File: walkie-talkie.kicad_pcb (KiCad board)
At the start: 2 copper layers, 50.5 x 74.5 mm, 12 parts, among them J1 I2C, J2 Conn_01x08, J3 esp32-pico-kit, J4 speakers, SW1 Transmit, SW2 POWER, U1 tp4056, U2 adafruit-MAX98357, U3 mems-mic

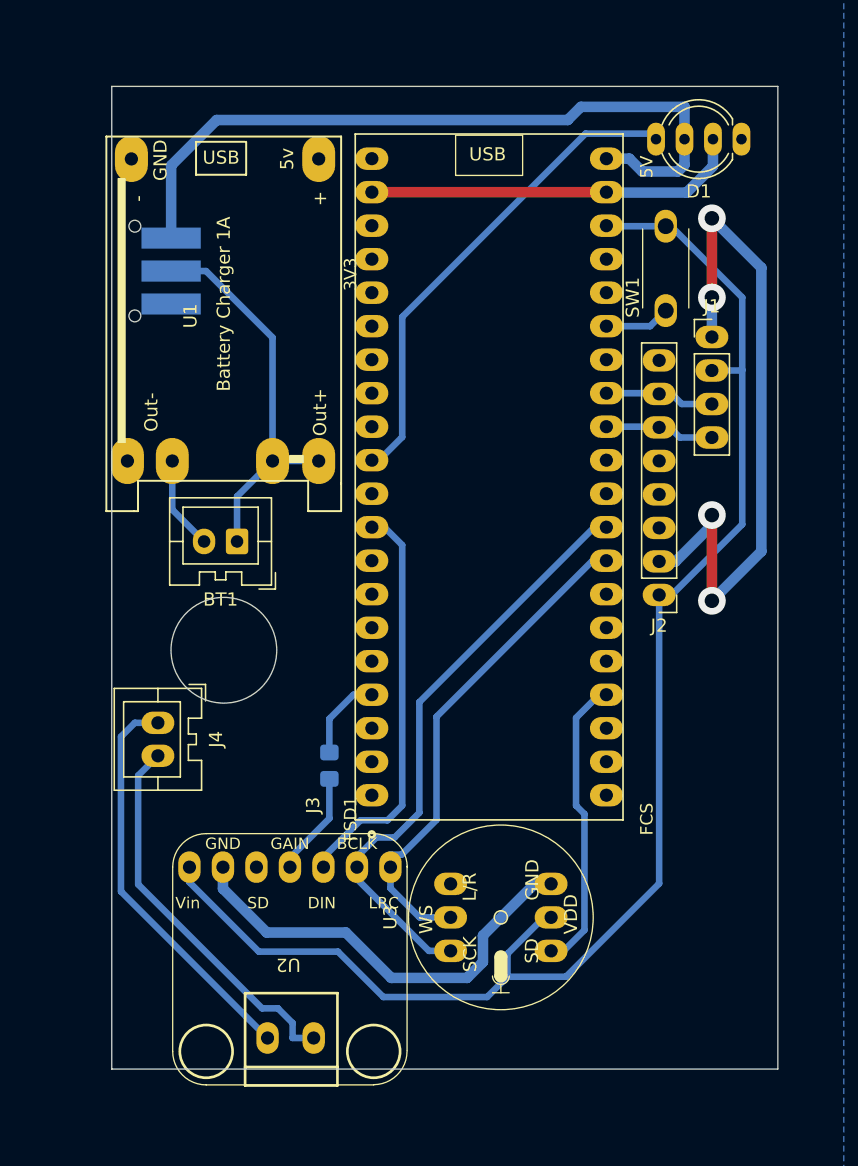
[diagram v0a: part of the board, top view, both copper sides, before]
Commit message: Add mounting holes
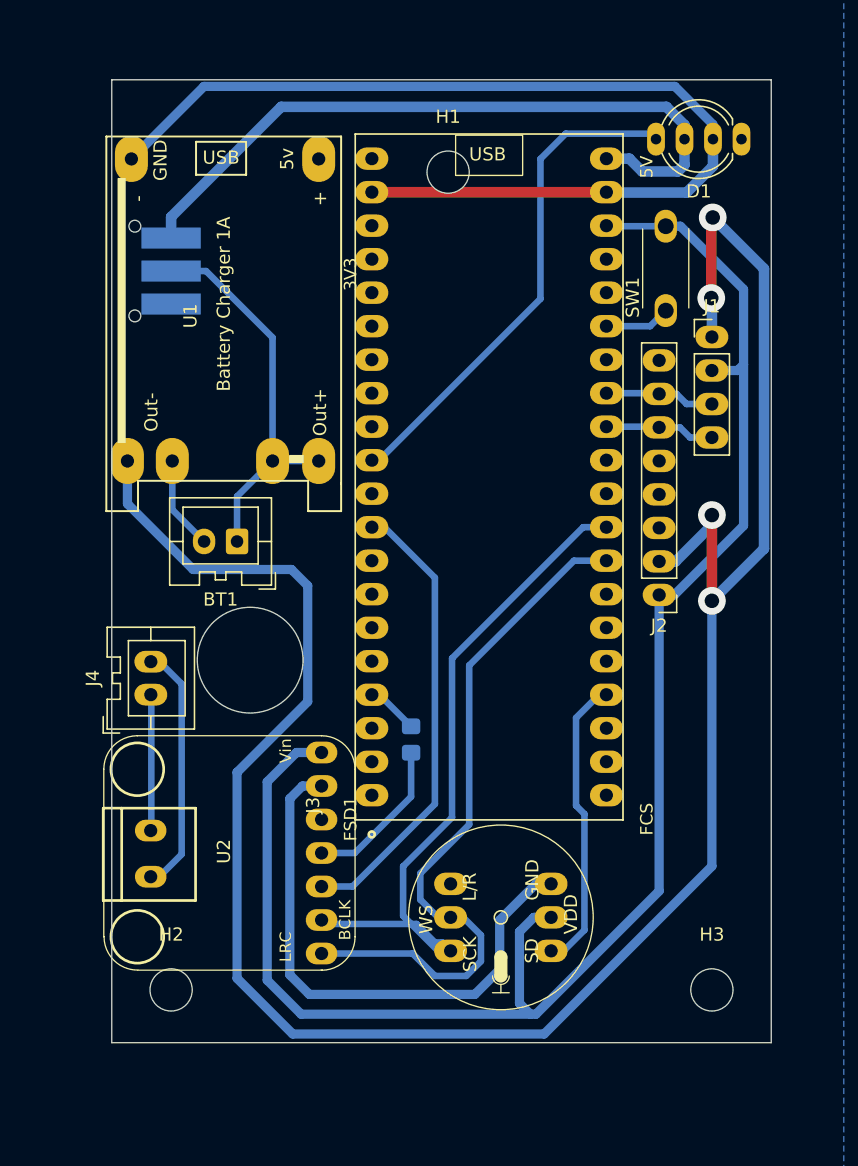
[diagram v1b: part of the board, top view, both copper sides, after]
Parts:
- added H1: MountingHole, MountingHole:MountingHole_3.2mm_M3, F.Cu at (68.0, 63.0)
- added H2: MountingHole, MountingHole:MountingHole_3.2mm_M3, F.Cu at (47.0, 125.0)
- added H3: MountingHole, MountingHole:MountingHole_3.2mm_M3, F.Cu at (88.0, 125.0)
- U1: value tp4056 -> WARNING: Switch off when Plugging in Power on the ESP
- moved U2 9.21 mm to (51.5, 114.5), turned to 90 degrees
- moved R1 6.50 mm to (65.2, 106.0)
- moved J4 2.20 mm to (45.5, 102.6), turned to 90 degrees
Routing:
- net GND: track 115.7 -> 288.1 mm
- net Net-(J4-Pin_1): track 30.7 -> 10.3 mm
- net I2S_RLCLK: track 38.2 -> 53.9 mm
- net +3V3: track 112.6 -> 128.1 mm
- net Net-(J4-Pin_2): track 29.2 -> 19.0 mm
- net I2S_BCLK: track 45.3 -> 52.3 mm
- net Net-(U2-GAIN): track 7.93 -> 11.9 mm
- net I2S_AMP_DATA: track 31.0 -> 34.7 mm
- net +5V: track 57.2 -> 54.1 mm
- net I2S_AMP_GAIN: track 6.53 -> 3.97 mm
- net Net-(D1-DIN): track 37.3 -> 38.2 mm
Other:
- board size 50.5 x 74.5 mm -> 50 x 73 mm

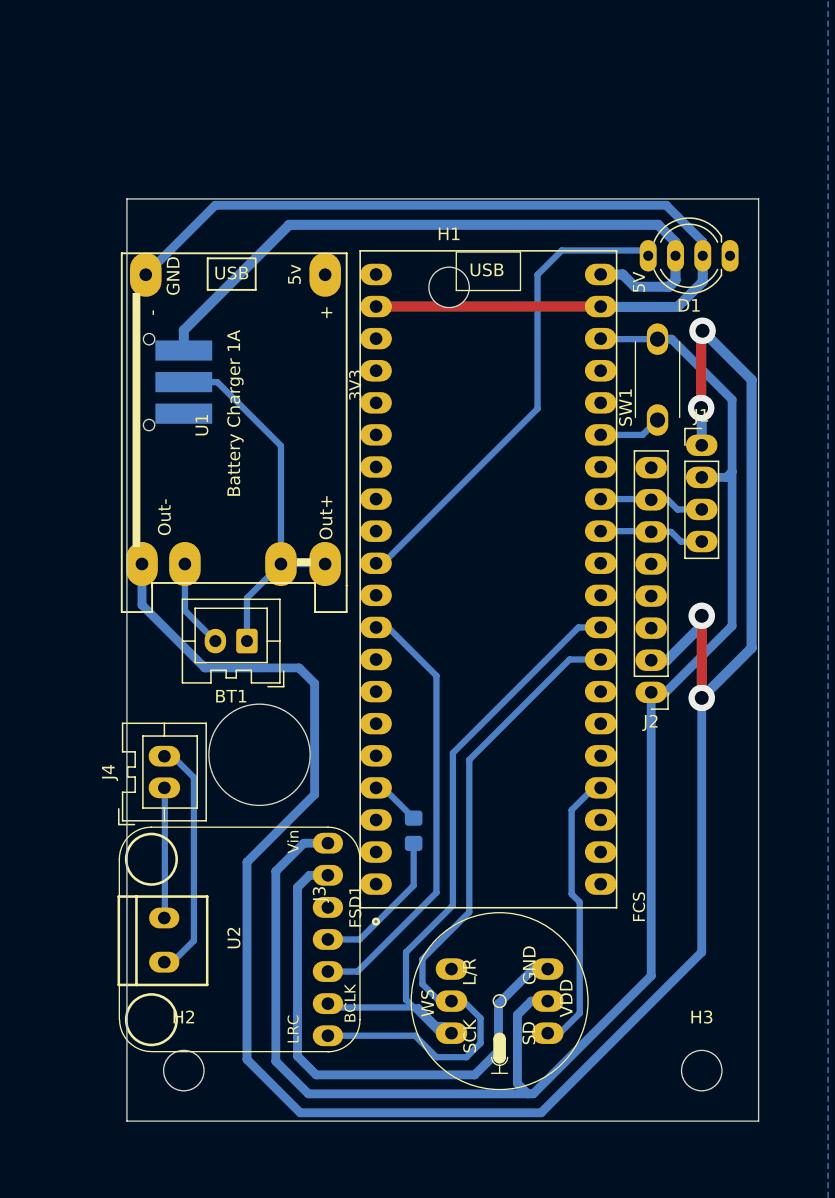
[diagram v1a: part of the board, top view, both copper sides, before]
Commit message: Add CVS speaker
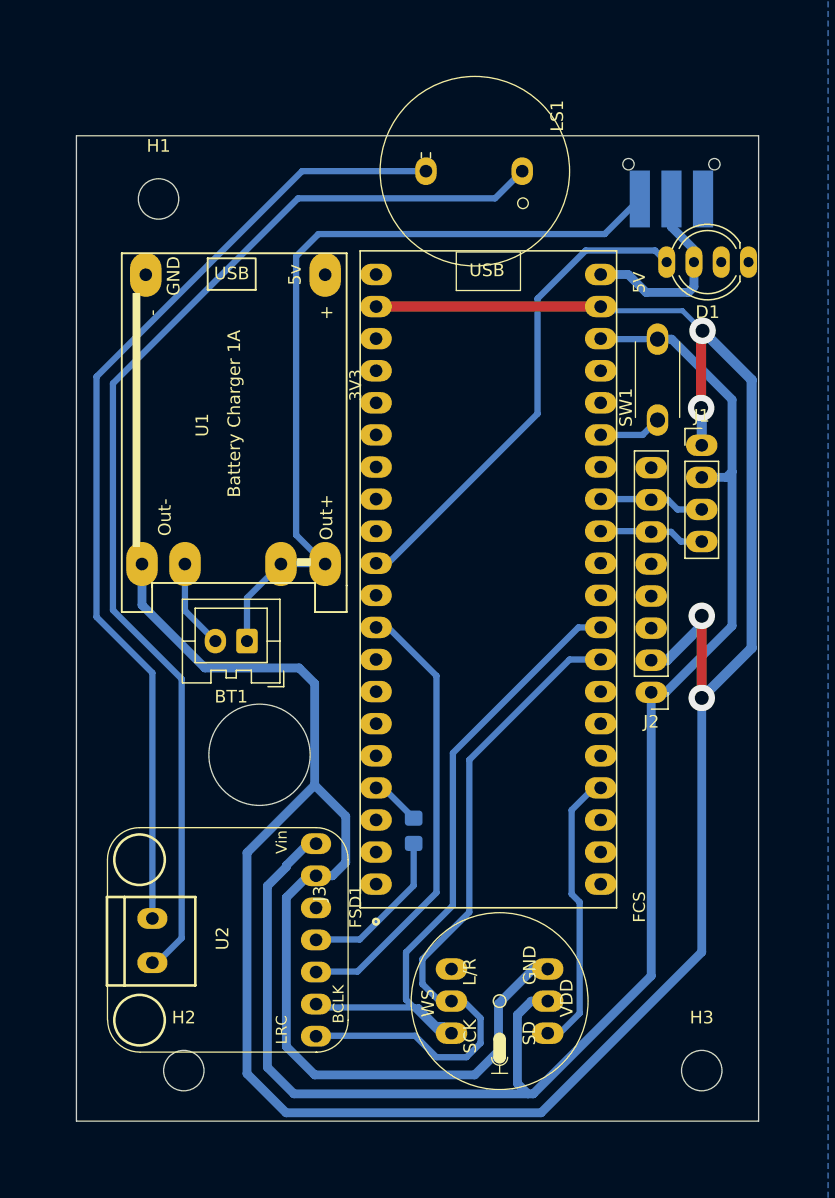
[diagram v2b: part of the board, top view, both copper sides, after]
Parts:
- removed J4: speakers, Connector_JST:JST_XA_B02B-XASK-1_1x02_P2.50mm_Vertical
- added LS1: Speaker, Connector_PinSocket_2.54mm:PinSocket_1x04_P2.54mm_Horizontal, F.Cu at (70.0, 53.8)
- moved SW2 44.8 mm to (85.6, 53.2), turned to 0 degrees
- moved H1 24.0 mm to (45.0, 56.0)
- moved D1 1.54 mm to (91.7, 61.0)
- moved U2 0.94 mm to (50.6, 114.5)
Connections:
- SW2 pad 1: unconnected-(SW2-A-Pad1) -> Net-(BT1-+)
- SW2 pad 2: Net-(BT1-+) -> +5V
- SW2 pad 3: +5V -> unconnected-(SW2-C-Pad3)
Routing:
- net Net-(U2-OUTP): track 19.0 -> 88.6 mm
- net Net-(U2-OUTN): track 10.3 -> 77.5 mm
- net GND: track 288.1 -> 248.4 mm
- net +5V: track 54.1 -> 15.8 mm
- net Net-(BT1-+): track 29.9 -> 65.1 mm
- net Net-(U2-GAIN): track 11.9 -> 12.8 mm
- net I2S_RLCLK: track 53.9 -> 54.9 mm
- net I2S_AMP_DATA: track 34.7 -> 35.7 mm
- net I2S_BCLK: track 52.3 -> 53.3 mm
- net Net-(D1-DIN): track 38.2 -> 39.0 mm
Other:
- board size 50 x 73 mm -> 54 x 78 mm

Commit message: Lolin32-Lite PCB
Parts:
- removed BT1: Battery_Cell, Connector_JST:JST_XA_B02B-XASK-1_1x02_P2.50mm_Vertical
- removed J2: Conn_01x08, Connector_PinHeader_2.54mm:PinHeader_1x08_P2.54mm_Vertical
- removed J3: esp32-pico-kit, esp32-pico-kit:esp32-pico-kit
- SW1: value Transmit -> POWER; footprint pts636:pts636 -> Button_Switch_SMD:SW_SPDT_CK-JS102011SAQN; moved to B.Cu
- SW2: value POWER -> Transmit; footprint Button_Switch_SMD:SW_SPDT_CK-JS102011SAQN -> pts636:pts636
- U1: value WARNING: Switch off when Plugging in Power on the ESP -> ~; footprint tp4056:tp4056 -> lolin32-lite:lolin32-lite
- moved H2 161.8 mm to (202.7, 81.0)
- moved U2 98.9 mm to (139.6, 71.7), turned to -90 degrees
- moved R1 73.1 mm to (129.8, 71.7)
- moved U3 71.7 mm to (137.9, 91.1), turned to 0 degrees
- moved H1 71.1 mm to (116.0, 59.0)
- moved LS1 67.8 mm to (137.9, 54.3)
- moved H3 65.7 mm to (147.0, 96.0)
- moved U1 65.0 mm to (116.0, 71.5), turned to 0 degrees
- moved SW2 62.2 mm to (147.4, 59.9), turned to 90 degrees
- moved D1 58.8 mm to (148.8, 46.7)
- moved SW1 39.9 mm to (116.3, 97.7), turned to 180 degrees
- moved J1 22.3 mm to (104.5, 90.5)
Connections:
- D1 pad 3: +5V -> +3V3
- SW1 pad 1: Net-(J3-IO2) -> +3V3
- SW1 pad 2: +3V3 -> Net-(SW1-B)
- SW2 pad 1: Net-(BT1-+) -> Net-(U1-IO22)
- SW2 pad 2: +5V -> +3V3
- U1 pad 1: VBUS -> unconnected-(U1-I36-Pad1)
- U1 pad 2: GND -> unconnected-(U1-I39-Pad2)
- U1 pad 3: Net-(BT1-+) -> Net-(SW1-B)
- U1 pad 4: Net-(BT1--) -> unconnected-(U1-I34-Pad4)
- U1 pad 5: Net-(BT1-+) -> unconnected-(U1-I35-Pad5)
- U1 pad 6: GND -> unconnected-(U1-IO32-Pad6)
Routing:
- net GND: track 248.4 -> 101.8 mm, vias 4 -> 6
- net Net-(U2-OUTP): track 88.6 -> 17.1 mm
- net Net-(BT1-+): track 65.1 -> 0.00 mm
- net Net-(U2-OUTN): track 77.5 -> 23.8 mm
- net Net-(U1-IO22): track 0.00 -> 47.0 mm
- net Net-(SW1-B): track 0.00 -> 41.2 mm
- net I2S_AMP_DATA: track 35.7 -> 5.34 mm
- net I2S_BCLK: track 53.3 -> 29.6 mm
- net I2S_RLCLK: track 54.9 -> 31.9 mm
- net I2C_SCL: track 8.34 -> 26.7 mm
- net +5V: track 15.8 -> 0.00 mm
- net I2S_MIC_DATA: track 22.6 -> 11.4 mm
- net I2C_SDA: track 8.34 -> 19.0 mm
- net Net-(D1-DIN): track 39.0 -> 28.8 mm
- net Net-(U2-GAIN): track 12.8 -> 3.45 mm
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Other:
- board size 54 x 78 mm -> 51 x 57 mm

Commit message: Plotting updates
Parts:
- removed the H2 at (202.7, 81.0)
- renumbered H3 to H2

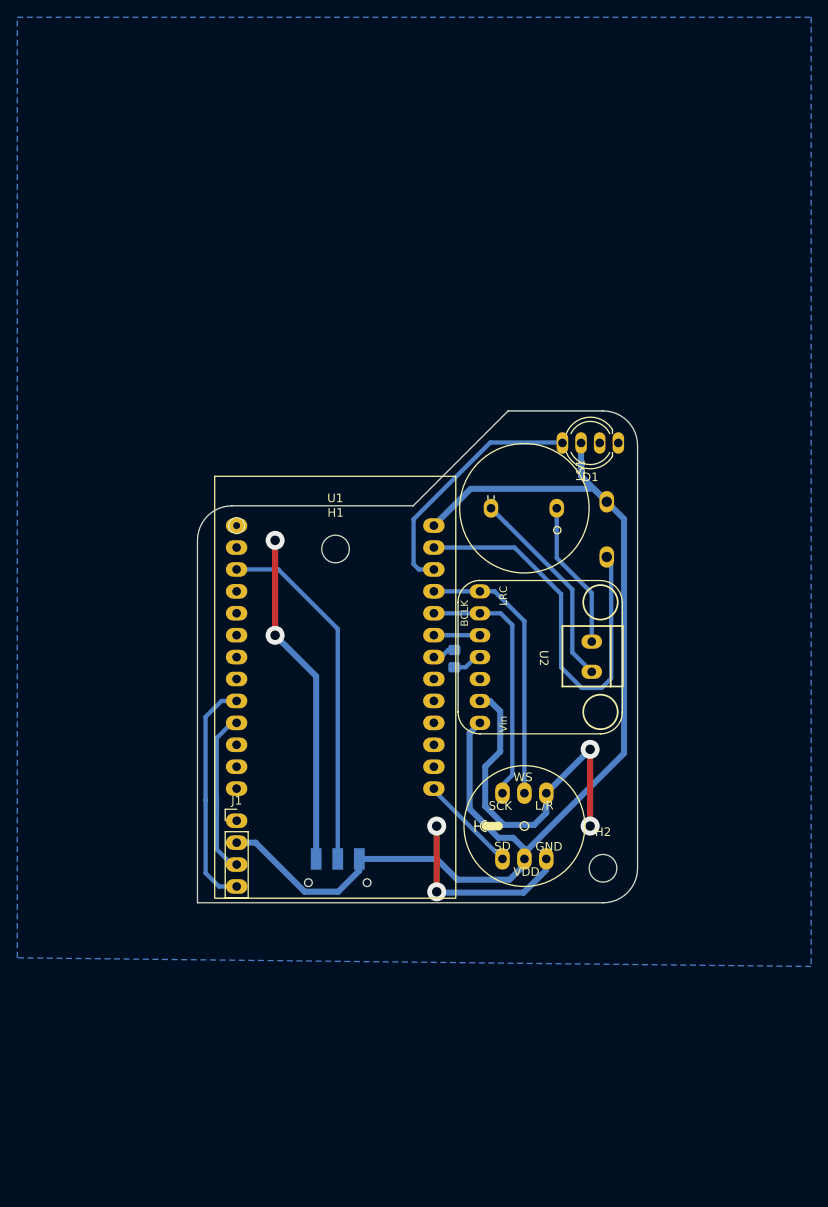
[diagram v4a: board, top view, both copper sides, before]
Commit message: Add components for new PCB
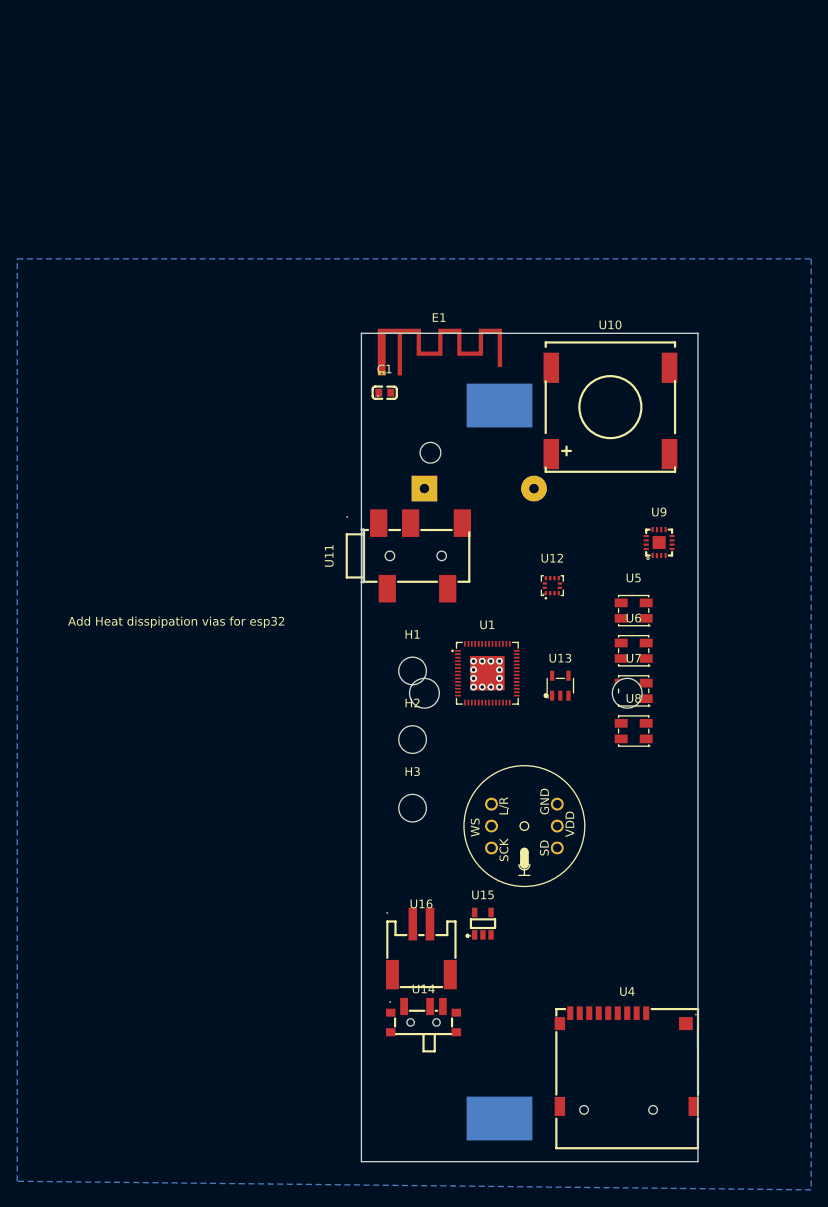
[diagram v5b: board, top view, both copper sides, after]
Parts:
- removed D1: NeoPixel_THT, LED_THT:LED_D5.0mm-4_RGB_Wide_Pins
- removed J1: I2C, Connector_PinHeader_2.54mm:PinHeader_1x04_P2.54mm_Vertical
- removed LS1: Speaker, Connector_PinSocket_2.54mm:PinSocket_1x04_P2.54mm_Horizontal
- removed R1: 100k, Resistor_SMD:R_0805_2012Metric_Pad1.20x1.40mm_HandSolder
- removed SW1: POWER, Button_Switch_SMD:SW_SPDT_CK-JS102011SAQN
- removed SW2: Transmit, pts636:pts636
- added BT1: Battery_Cell, Battery:BatteryHolder_Keystone_2479_3xAAA, B.Cu at (126.3, 52.0)
- added C1: 5.6p, jlc_footprints:C0603, F.Cu at (121.7, 40.9)
- added E1: Antenna_Trace, RF_Antenna:Texas_SWRA117D_2.4GHz_Right, F.Cu at (123.5, 38.6)
- added H3: MountingHole, MountingHole:MountingHole_3.2mm_M3, F.Cu at (124.9, 89.0)
- added U10: FS-1540, jlc_footprints:BUZ-SMD_5P-L15.0-W15.0-P13.7-BL, F.Cu at (147.9, 43.0)
- added U11: PJ-327A_5JJ, jlc_footprints:AUDIO-SMD_PJ-327A5JJ, F.Cu at (125.9, 59.8)
- added U12: LIS2DH12TR, jlc_footprints:LGA-12_L2.0-W2.0-P0.50-BL, F.Cu at (141.1, 63.2)
- added U13: MCP73831T-2ACI_OT, jlc_footprints:SOT-23-5_L3.0-W1.7-P0.95-LS2.8-BL, F.Cu at (142.1, 74.8)
- added U14: ON, jlc_footprints:SW-SMD_MK-12C02-G020, F.Cu at (126.2, 113.5)
- added U15: AP2112K-3_3TRG1, jlc_footprints:SOT-25-5_L2.9-W1.6-P0.95-LS2.8-BL, F.Cu at (133.1, 102.4)
- added U16: +, jlc_footprints:CONN-SMD_P2.00_S2B-PH-SM4-TB-LF-SN, F.Cu at (126.0, 105.4)
- added U4: TF-115, jlc_footprints:TF-SMD_TF-115, F.Cu at (149.8, 118.2)
- added U5: SK6812MINI-HS, jlc_footprints:LED-SMD_4P-L3.5-W3.5-BR_SK6812MINI-HS, F.Cu at (150.5, 66.1)
- added U6: SK6812MINI-HS, jlc_footprints:LED-SMD_4P-L3.5-W3.5-BR_SK6812MINI-HS, F.Cu at (150.5, 70.8)
- added U7: SK6812MINI-HS, jlc_footprints:LED-SMD_4P-L3.5-W3.5-BR_SK6812MINI-HS, F.Cu at (150.5, 75.4)
- added U8: SK6812MINI-HS, jlc_footprints:LED-SMD_4P-L3.5-W3.5-BR_SK6812MINI-HS, F.Cu at (150.5, 80.1)
- added U9: MAX98357AETE+T, jlc_footprints:TQFN-16_L3.0-W3.0-P0.50-BL-EP1.5, F.Cu at (153.5, 58.3)
- U1: value ~ -> ESP32-S3(R8); footprint lolin32-lite:lolin32-lite -> jlc_footprints:QFN-56_L7.0-W7.0-P0.40-TL-EP4.0
- U2: value adafruit-MAX98357 -> BH-18650-B1BA002; footprint adafruit-MAX98357:adafruit-MAX98357 -> jlc_footprints:BATTERY-SMD_18650-1S-L77.1-W20.7-1; moved to B.Cu
- moved H2 26.6 mm to (124.9, 81.1)
- moved U1 17.7 mm to (133.6, 73.4)
- moved H1 16.7 mm to (124.9, 73.1)
- moved U2 12.9 mm to (135.0, 83.7), turned to 180 degrees
- turned U3 to 90 degrees
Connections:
- U1 pad 10: I2C_SDA -> unconnected-(U1-GPIO5-Pad10)
- U1 pad 13: GND -> unconnected-(U1-GPIO8-Pad13)
- U1 pad 14: I2S_MIC_DATA -> unconnected-(U1-GPIO9-Pad14)
- U1 pad 20: I2S_AMP_GAIN -> unconnected-(U1-VDD3P3_RTC-Pad20)
- U1 pad 21: I2S_AMP_DATA -> unconnected-(U1-XTAL_32K_P-Pad21)
- U1 pad 22: I2S_BCLK -> unconnected-(U1-XTAL_32K_N-Pad22)
- U1 pad 23: I2S_RLCLK -> unconnected-(U1-GPIO17-Pad23)
- U1 pad 24: Net-(D1-DIN) -> unconnected-(U1-GPIO18-Pad24)
- U1 pad 25: Net-(U1-IO22) -> unconnected-(U1-GPIO19-Pad25)
- U1 pad 26: +3V3 -> unconnected-(U1-GPIO20-Pad26)
- U1 pad 3: Net-(SW1-B) -> unconnected-(U1-VDD3P3-Pad3)
- U1 pad 9: I2C_SCL -> unconnected-(U1-GPIO4-Pad9)
- U2 pad 1: +3V3 -> unconnected-(U2-Pad1)
- U2 pad 2: GND -> unconnected-(U2-Pad2)
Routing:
- net +3V3: track 137.4 -> 0.00 mm
- net GND: track 101.8 -> 0.00 mm, vias 6 -> 0
- net Net-(U1-IO22): track 47.0 -> 0.00 mm
- net Net-(SW1-B): track 41.2 -> 0.00 mm
- net I2S_RLCLK: track 31.9 -> 0.00 mm
- net I2S_BCLK: track 29.6 -> 0.00 mm
- net Net-(D1-DIN): track 28.8 -> 0.00 mm
- net I2C_SCL: track 26.7 -> 0.00 mm
- net Net-(U2-OUTN): track 23.8 -> 0.00 mm
- net I2C_SDA: track 19.0 -> 0.00 mm
- net Net-(U2-OUTP): track 17.1 -> 0.00 mm
- net I2S_MIC_DATA: track 11.4 -> 0.00 mm
- net I2S_AMP_DATA: track 5.34 -> 0.00 mm
- net Net-(U2-GAIN): track 3.45 -> 0.00 mm
- net I2S_AMP_GAIN: track 2.71 -> 0.00 mm
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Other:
- board size 51 x 57 mm -> 39 x 96 mm
- board text added: "Add Heat disspipation vias for esp32"

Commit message: WIP
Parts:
- added J1: I2C, jlc_footprints:CONN-SMD_BM04B-SRSS-TB, F.Cu at (153.7, 45.2)
- added JP1: USB_B_Micro, jlc_footprints:MICRO-USB-SMD_1050171001, F.Cu at (146.5, 37.4)
- added U17: W25Q128JVSIQTR, jlc_footprints:SOIC-8_L5.3-W5.3-P1.27-LS8.0-BL, F.Cu at (133.0, 82.0)
- added X1: X322540MPB4SI, jlc_footprints:OSC-SMD_4P-L3.2-W2.5-BL_SIT8008BI, F.Cu at (132.9, 66.1)
- U16: moved to B.Cu
- moved E1 87.9 mm to (124.6, 126.5), turned to 90 degrees
- moved C1 87.3 mm to (128.0, 128.0)
- moved U16 54.6 mm to (147.0, 55.0), turned to 180 degrees
- moved U14 39.9 mm to (155.0, 85.9), turned to 90 degrees
- moved U3 27.0 mm to (135.2, 118.0)
- moved U11 18.8 mm to (125.0, 41.0), turned to 0 degrees
- moved U10 7.91 mm to (140.0, 42.0)
- moved U2 3.02 mm to (138.0, 84.0)
- moved U1 0.20 mm to (133.6, 73.2)
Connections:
- U1 pad 25: unconnected-(U1-GPIO19-Pad25) -> USB_N
- U1 pad 26: unconnected-(U1-GPIO20-Pad26) -> USB_P
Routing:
- net unconnected-(U1-GND-Pad57): vias 12 -> 0
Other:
- board size 39 x 96 mm -> 38 x 96 mm
